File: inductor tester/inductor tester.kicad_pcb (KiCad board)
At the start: 2 copper layers, 50 x 50 mm, 40 parts, among them P101 I Sense, P102 Inductor Under Test, P103 V Sense, P104 10V_In, P105 0V_In, Q101 BC847, Q102 PSMN4R3-30BL, SW101 SW_PUSH, U102 LM555N

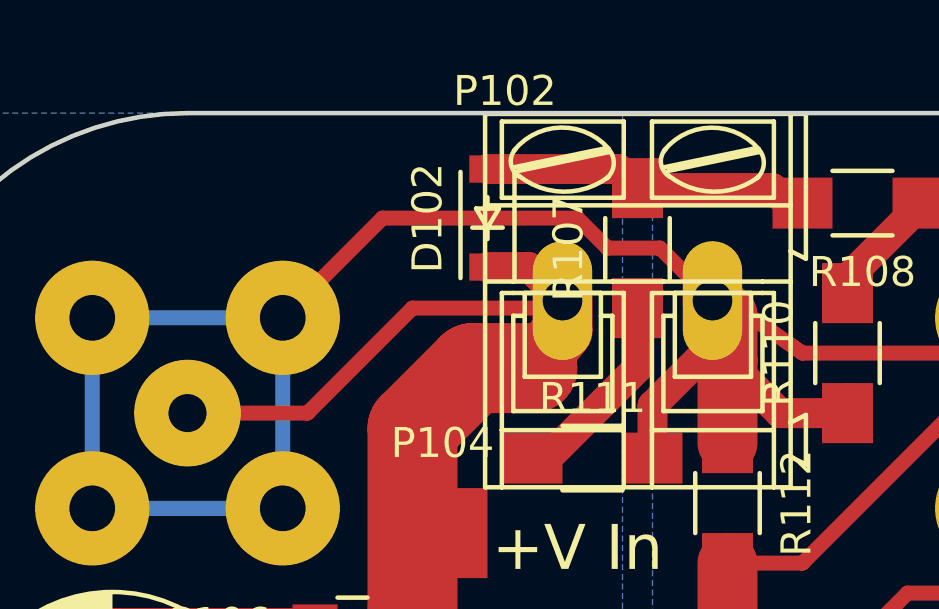
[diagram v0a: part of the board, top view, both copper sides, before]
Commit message: Added notes on exporting, saved PCB as ordered.
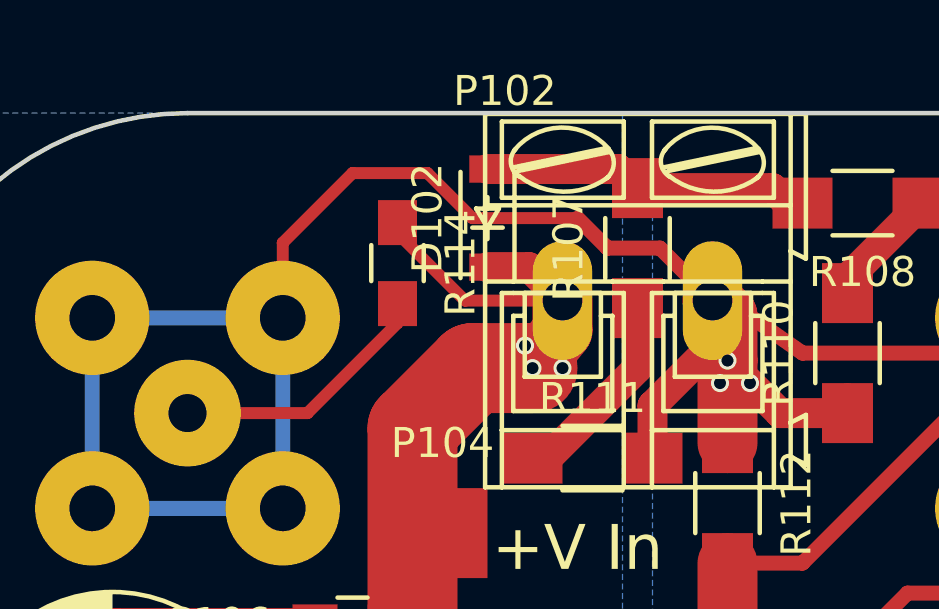
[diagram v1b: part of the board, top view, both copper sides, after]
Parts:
- added R114: 50, Resistors_SMD:R_0805_HandSoldering, F.Cu at (107.0, 105.0)
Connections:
- P103 pad 1: VCC -> Net-(P103-Pad1)
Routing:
- net Net-(P103-Pad1): track 0.00 -> 8.89 mm
- net Net-(P101-Pad2): track 95.0 -> 99.9 mm, vias 0 -> 3
- net VCC: track 148.6 -> 144.4 mm, vias 0 -> 3
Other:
- board text added: "5-15 VDC"
- board text removed: "5-15VDC"
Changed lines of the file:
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@@
 (kicad_pcb (version 4) (host pcbnew 4.0.2-stable)
   (general
-    (links 75)
+    (links 76)
     (no_connects 0)
-    (area 89.924999 99.924999 140.075001 150.075001)
+    (area 89.924999 97.5 140.632143 151.375)
     (thickness 1.6)
     (drawings 18)
-    (tracks 213)
+    (tracks 234)
     (zones 0)
-    (modules 40)
-    (nets 18)
+    (modules 41)
+    (nets 19)
   )
   (page A4)
   (layers
     (0 F.Cu signal)
-    (31 B.Cu signal)
+    (31 B.Cu signal hide)
     (32 B.Adhes user)
     (33 F.Adhes user)
-    (34 B.Paste user hide)
+    (34 B.Paste user)
     (35 F.Paste user)
     (36 B.SilkS user)
     (37 F.SilkS user)
-    (38 B.Mask user)
+    (38 B.Mask user hide)
     (39 F.Mask user)
     (40 Dwgs.User user)
@@
   )
   (setup
-    (last_trace_width 0.2)
+    (last_trace_width 0.4)
     (user_trace_width 0.2)
     (user_trace_width 0.3)
@@
     (via_min_size 0.4)
     (via_min_drill 0.3)
+    (user_via 0.5 0.35)
     (uvia_size 0.3)
     (uvia_drill 0.1)
@@
     (aux_axis_origin 90 100)
     (grid_origin 90 100)
-    (visible_elements FFFFFF7F)
+    (visible_elements FFFFFFFF)
     (pcbplotparams
-      (layerselection 0x00030_80000001)
+      (layerselection 0x010f8_80000001)
       (usegerberextensions false)
       (excludeedgelayer true)
@@
       (outputformat 1)
       (mirror false)
-      (drillshape 1)
+      (drillshape 0)
       (scaleselection 1)
-      (outputdirectory ""))
+      (outputdirectory gerbers/))
   )
   (net 0 "")
@@
   (net 16 "Net-(R102-Pad2)")
   (net 17 "Net-(R108-Pad1)")
+  (net 18 "Net-(P103-Pad1)")
   (net_class Default "This is the default net class."
     (clearance 0.2)
@@
     (add_net "Net-(D102-Pad2)")
     (add_net "Net-(P101-Pad2)")
+    (add_net "Net-(P103-Pad1)")
     (add_net "Net-(Q101-Pad1)")
     (add_net "Net-(Q101-Pad3)")
@@
       (net 8 "Net-(P101-Pad2)"))
     (pad 1 thru_hole circle (at 0 0 90) (size 3.556 3.556) (drill 1.27) (layers *.Cu *.Mask B.SilkS)
-      (net 2 VCC))
+      (net 18 "Net-(P103-Pad1)"))
     (pad 2 thru_hole circle (at 3.175 3.175 90) (size 3.81 3.81) (drill 1.524) (layers *.Cu *.Mask B.SilkS)
       (net 8 "Net-(P101-Pad2)"))
@@
     )
   )
-  (gr_text 5-15VDC (at 118.5 147) (layer B.SilkS)
+  (module Resistors_SMD:R_0805_HandSoldering (layer F.Cu)
+    (at 107 105 270)
+    (descr "Resistor SMD 0805, hand soldering")
+    (tags "resistor 0805")
+    (attr smd)
+    (fp_text reference R114 (at 0 -2.1 270) (layer F.SilkS)
+      (effects (font (size 1 1) (thickness 0.15)))
+    )
+    (fp_text value 50 (at 0 2.1 270) (layer F.Fab)
+      (effects (font (size 1 1) (thickness 0.15)))
+    )
+    (fp_line (start -2.4 -1) (end 2.4 -1) (layer F.CrtYd) (width 0.05))
+    (fp_line (start -2.4 1) (end 2.4 1) (layer F.CrtYd) (width 0.05))
+    (fp_line (start -2.4 -1) (end -2.4 1) (layer F.CrtYd) (width 0.05))
+    (fp_line (start 2.4 -1) (end 2.4 1) (layer F.CrtYd) (width 0.05))
+    (fp_line (start 0.6 0.875) (end -0.6 0.875) (layer F.SilkS) (width 0.15))
+    (fp_line (start -0.6 -0.875) (end 0.6 -0.875) (layer F.SilkS) (width 0.15))
+    (pad 1 smd rect (at -1.35 0 270) (size 1.5 1.3) (layers F.Cu F.Paste F.Mask)
+      (net 2 VCC))
+    (pad 2 smd rect (at 1.35 0 270) (size 1.5 1.3) (layers F.Cu F.Paste F.Mask)
+      (net 18 "Net-(P103-Pad1)"))
+    (model Resistors_SMD.3dshapes/R_0805_HandSoldering.wrl
+      (at (xyz 0 0 0))
+      (scale (xyz 1 1 1))
+      (rotate (xyz 0 0 0))
+    )
+  )
+  (gr_text "5-15\nVDC" (at 120 145) (layer B.SilkS)
     (effects (font (size 3 2) (thickness 0.3)) (justify mirror))
   )
@@
   (segment (start 130.49886 132.00114) (end 130.75 131.75) (width 0.2) (layer F.Cu) (net 1) (status 30))
   (segment (start 134 128.75) (end 134.25 128.75) (width 0.4) (layer F.Cu) (net 1) (status 30))
+  (segment (start 111.25 107.75) (end 111.25 108.5) (width 0.4) (layer F.Cu) (net 2))
+  (via (at 111.25 107.75) (size 0.6) (drill 0.4) (layers F.Cu B.Cu) (net 2))
+  (segment (start 111.25 108.5) (end 109.5 108.5) (width 3) (layer F.Cu) (net 2))
+  (via (at 111.5 108.5) (size 0.6) (drill 0.4) (layers F.Cu B.Cu) (net 2))
+  (segment (start 112.5 108.5) (end 111.5 108.5) (width 0.4) (layer F.Cu) (net 2))
+  (via (at 112.5 108.5) (size 0.6) (drill 0.4) (layers F.Cu B.Cu) (net 2))
+  (segment (start 111.5 108.5) (end 112.5 108.5) (width 0.4) (layer B.Cu) (net 2))
+  (segment (start 111.5 108.5) (end 111.25 108.5) (width 3) (layer F.Cu) (net 2))
+  (segment (start 112.5 106.25) (end 109.25 106.25) (width 0.4) (layer F.Cu) (net 2))
+  (segment (start 109.25 106.25) (end 107 104) (width 0.4) (layer F.Cu) (net 2))
+  (segment (start 107 104) (end 107 103.65) (width 0.4) (layer F.Cu) (net 2))
   (segment (start 110 105.135) (end 111.385 105.135) (width 1) (layer F.Cu) (net 2))
   (segment (start 111.385 105.135) (end 112.5 106.25) (width 1) (layer F.Cu) (net 2))
-  (segment (start 112.25 106.5) (end 107.5 106.5) (width 0.5) (layer F.Cu) (net 2))
-  (segment (start 104 110) (end 107.5 106.5) (width 0.5) (layer F.Cu) (net 2))
-  (segment (start 104 110) (end 100 110) (width 0.5) (layer F.Cu) (net 2))
   (segment (start 112.25 106.5) (end 112.5 106.25) (width 0.5) (layer F.Cu) (net 2))
   (segment (start 121.65 129.5) (end 123 129.5) (width 0.5) (layer F.Cu) (net 2))
@@
   (segment (start 100 121) (end 107.5 121) (width 2) (layer F.Cu) (net 2))
   (segment (start 109.5 108.5) (end 107.5 110.5) (width 3) (layer F.Cu) (net 2))
-  (segment (start 111.5 108.5) (end 109.5 108.5) (width 3) (layer F.Cu) (net 2))
   (segment (start 112.5 107.25) (end 111.5 108.5) (width 2) (layer F.Cu) (net 2) (status 10))
   (segment (start 107.5 125) (end 106.5 126) (width 3) (layer F.Cu) (net 2))
@@
   (segment (start 110 101.865) (end 114.365 101.865) (width 1) (layer F.Cu) (net 7) (status 20))
   (segment (start 114.365 101.865) (end 115 102.5) (width 1) (layer F.Cu) (net 7) (status 30))
-  (segment (start 103.175 106.825) (end 106.5 103.5) (width 0.5) (layer F.Cu) (net 8))
-  (segment (start 115.75 104.5) (end 117.5 106.25) (width 0.5) (layer F.Cu) (net 8))
+  (via (at 118 108.25) (size 0.6) (drill 0.4) (layers F.Cu B.Cu) (net 8))
+  (segment (start 118.5 108.75) (end 118.75 109) (width 0.4) (layer B.Cu) (net 8))
+  (via (at 118.75 109) (size 0.6) (drill 0.4) (layers F.Cu B.Cu) (net 8))
+  (segment (start 117.75 109) (end 118.75 109) (width 0.4) (layer F.Cu) (net 8))
+  (via (at 117.75 109) (size 0.6) (drill 0.4) (layers F.Cu B.Cu) (net 8))
+  (segment (start 117.75 108.5) (end 117.75 109) (width 0.4) (layer B.Cu) (net 8))
+  (segment (start 117.75 108.5) (end 118 108.25) (width 0.4) (layer B.Cu) (net 8))
+  (segment (start 103.175 104.325) (end 103.175 106.825) (width 0.4) (layer F.Cu) (net 8))
+  (segment (start 105.5 102) (end 103.175 104.325) (width 0.4) (layer F.Cu) (net 8))
+  (segment (start 108 102) (end 105.5 102) (width 0.4) (layer F.Cu) (net 8))
+  (segment (start 109.5 103.5) (end 108 102) (width 0.4) (layer F.Cu) (net 8))
+  (segment (start 113 103.5) (end 109.5 103.5) (width 0.4) (layer F.Cu) (net 8))
+  (segment (start 113 103.5) (end 114 104.5) (width 0.5) (layer F.Cu) (net 8))
   (segment (start 114 104.5) (end 115.75 104.5) (width 0.5) (layer F.Cu) (net 8))
-  (segment (start 113 103.5) (end 114 104.5) (width 0.5) (layer F.Cu) (net 8))
-  (segment (start 106.5 103.5) (end 113 103.5) (width 0.5) (layer F.Cu) (net 8))
+  (segment (start 117.5 106.25) (end 115.75 104.5) (width 0.5) (layer F.Cu) (net 8))
   (segment (start 122 110) (end 119.75 110) (width 1) (layer F.Cu) (net 8))
   (segment (start 119.75 110) (end 118 108.25) (width 1) (layer F.Cu) (net 8))
+  (segment (start 118 108.25) (end 118 108.25) (width 1) (layer F.Cu) (net 8))
   (segment (start 115.5 111.5) (end 115.5 109.75) (width 1) (layer F.Cu) (net 8))
   (segment (start 115.5 109.75) (end 117.5 107.75) (width 1) (layer F.Cu) (net 8))
@@
   (segment (start 122 106) (end 122 105.5) (width 1) (layer F.Cu) (net 17))
   (segment (start 122 105.5) (end 124.5 103) (width 1) (layer F.Cu) (net 17))
+  (segment (start 100 110) (end 104 110) (width 0.4) (layer F.Cu) (net 18))
+  (segment (start 104 110) (end 107 107) (width 0.4) (layer F.Cu) (net 18))
+  (segment (start 107 107) (end 107 106.35) (width 0.4) (layer F.Cu) (net 18))
   (zone (net 2) (net_name VCC) (layer B.Cu) (hatch edge 0.508)
     (connect_pads yes (clearance 0.508))
@@
       )
     )
+  )
+  (zone (net 0) (net_name "") (layer B.Mask) (hatch edge 0.508)
+    (connect_pads (clearance 0.508))
+    (min_thickness 0.254)
+    (fill yes (arc_segments 16) (thermal_gap 0.508) (thermal_bridge_width 0.508))
+    (polygon
+      (pts
+        (xy 107.5 97.5) (xy 122.5 97.5) (xy 122.5 140) (xy 107.5 140) (xy 107.5 100)
+      )
+    )

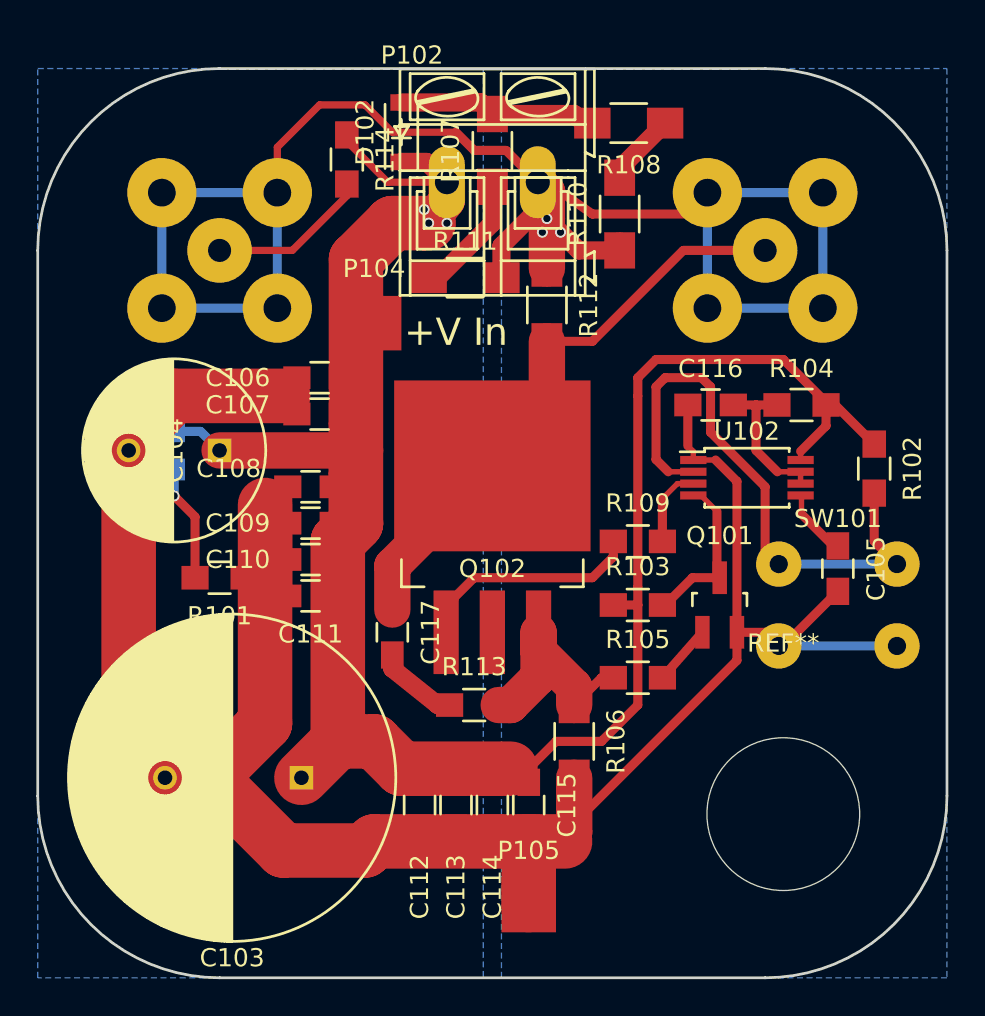
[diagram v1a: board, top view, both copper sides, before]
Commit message: PCB v2 - several changes:
  * Fixed reset issue that caused current limit oscillation
  * Switched 555 to an easier-to-solder footprint
  * Better silkscreen labelling
  * Improved BNC footprints to accept wider variety of connectors
  * Thermal relief for through hole pads
  * Added OSHW logo
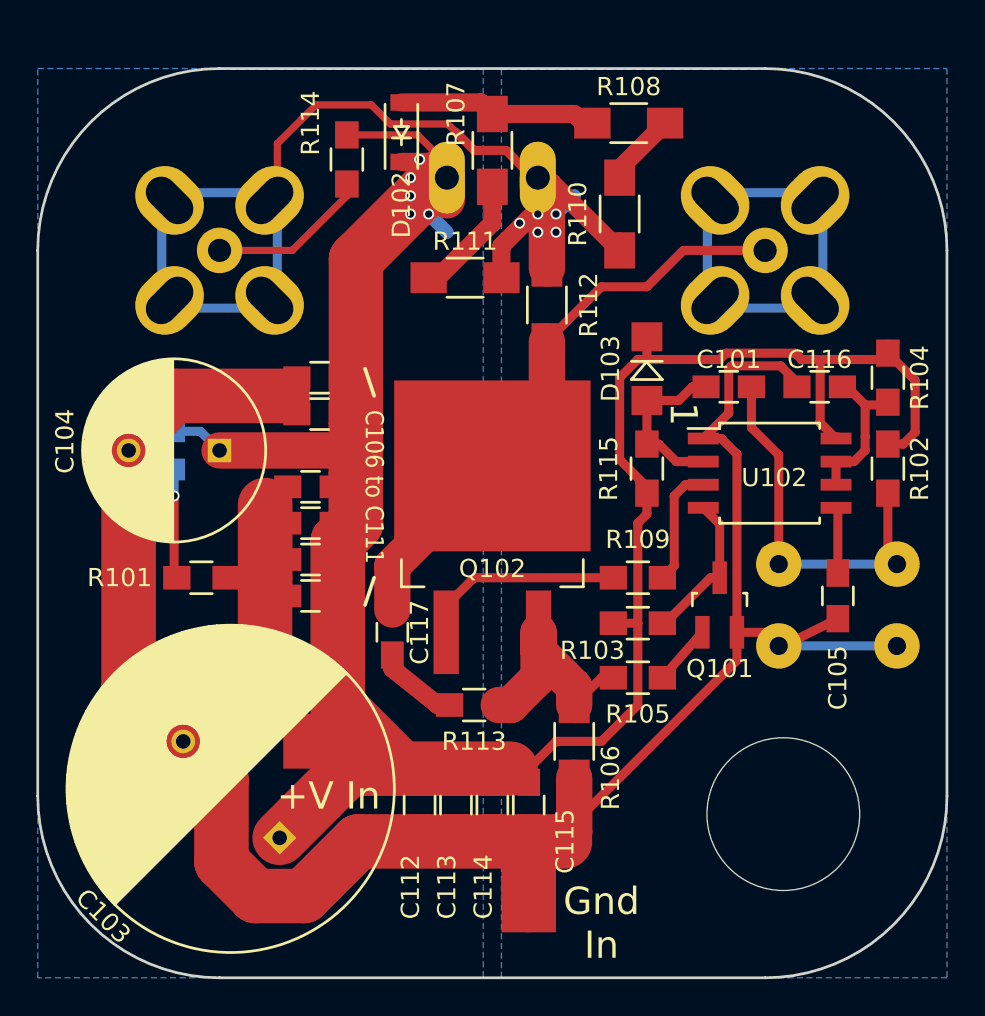
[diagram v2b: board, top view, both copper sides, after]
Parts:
- added C101: 100nF, Capacitors_SMD:C_0805_HandSoldering, F.Cu at (128.0, 117.5)
- added D103: 1N4148, Diodes_SMD:MiniMELF_Standard, F.Cu at (123.5, 116.5)
- added R115: 10k, Resistors_SMD:R_0805_HandSoldering, F.Cu at (123.5, 122.0)
- added REF**: Symbol_OSHW-Logo_SilkScreen, Symbols:Symbol_OSHW-Logo_SilkScreen, B.Cu at (98.0, 137.0)
- added REF**: barrel polarity, Symbols:barrel_polarity, B.Cu at (120.0, 146.0)
- P101: footprint Connect:bnc-ci -> slotted_bnc:bnc-ci
- P102, SW101: moved to B.Cu
- U102: footprint Housings_SSOP:TSSOP-8_4.4x3mm_Pitch0.65mm -> Housings_SOIC:SOIJ-8_5.3x5.3mm_Pitch1.27mm
- moved P104 23.3 mm to (105.0, 137.0)
- moved C116 6.08 mm to (133.0, 117.5)
- moved R104 4.98 mm to (136.8, 117.0), turned to 270 degrees
- moved C103 3.51 mm to (103.3, 142.3), turned to 135 degrees
- moved R109 2.00 mm to (123.0, 128.0)
- moved C105 1.50 mm to (134.0, 129.0)
- moved U102 1.27 mm to (130.2, 122.2)
- moved R101 1.00 mm to (99.0, 128.0)
- moved R103 1.00 mm to (123.0, 130.5)
- moved R102 0.75 mm to (136.8, 122.0)
- turned SW101 to 180 degrees
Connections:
- R102 pad 2: Net-(R102-Pad2) -> Net-(C101-Pad2)
- SW101 pad 2: Net-(R102-Pad2) -> Net-(C101-Pad2)
- U102 pad 2: Net-(R102-Pad2) -> Net-(C101-Pad1)
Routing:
- net VCC: track 144.4 -> 176.7 mm, vias 3 -> 5
- net Net-(R102-Pad2): track 32.0 -> 0.00 mm
- net Net-(C101-Pad2): track 0.00 -> 22.0 mm
- net Net-(C101-Pad1): track 0.00 -> 9.46 mm
- net GND: track 141.0 -> 147.5 mm
- net Net-(P101-Pad2): track 99.9 -> 97.3 mm, vias 3 -> 5
- net Net-(R109-Pad2): track 4.39 -> 6.62 mm
- net Net-(Q102-Pad1): track 12.6 -> 11.3 mm
- net Net-(Q101-Pad3): track 9.36 -> 8.62 mm
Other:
- board text added: "+"
- board text added: "-"
- board text added: "1"
- board text added: "10mV/A"
- board text added: "C106 to C111"
- board text added: "Gnd In"
- board text added: "I"
- board text added: "V"
